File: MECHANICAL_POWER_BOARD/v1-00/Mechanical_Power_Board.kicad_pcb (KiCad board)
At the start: 2 copper layers, 180.4 x 44.5 mm, 46 parts, among them K1 COLONETTE, K10 CONN_3, K11 CONN_3, K12 CONN_3, K13 CONN_3, K14 CONN_3, K15 CONN_3, K16 CONN_3, K17 CONN_3, K18 CONN_3, K19 CONN_3, K2 COLONETTE, K20 CONN_3, K3 COLONETTE, K4 COLONETTE, K5 COLONETTE, K6 COLONETTE, K7 COLONETTE, K8 COLONETTE, K9 CONN_3, P1 CONN_12, P10 CONN_4, P11 CONN_4, P12 CONN_6, P13 CONN_6, P14 CONN_8, P15 CONN_8X2, P16 CONN_6, P17 CONN_8X2, P18 CONN_5X2, P19 CONN_5X2, P2 HE10-40, P3 CONN_4, P4 CONN_4, P5 CONN_4, P6 CONN_4

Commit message: Mechanical Power Board V1-00 ready for production
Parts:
- removed P14: CONN_8, KK-8-H
- removed P16: CONN_6, WEIDMULLER6
- added D6: 3V6, Diodes_SMD:MELF_Handsoldering, B.Cu at (107.3, 43.9)
- added D7: 5V6, Diodes_SMD:MELF_Handsoldering, B.Cu at (103.8, 43.9)
- added D8: 5V6, Diodes_SMD:MELF_Handsoldering, B.Cu at (100.2, 43.9)
- added D9: 13V, Diodes_SMD:MELF_Handsoldering, B.Cu at (96.6, 43.9)
- added K21: CONN_2, CEN-PCB:KK-2, F.Cu at (134.0, 52.1)
- added K22: CONN_2, CEN-PCB:KK-2, F.Cu at (148.0, 52.1)
- added K23: CONN_3, CEN-PCB:KK-3, F.Cu at (155.6, 52.1)
- added K24: CONN_3, CEN-PCB:KK-3, F.Cu at (141.6, 52.1)
- R1: value 1K -> 4.7k
- R2: value 820 -> 4.7k
- R3: value 680 -> 1.5k
- R4: value 330 -> 1.5k
- R5: value 220 -> 680
- moved P12 18.7 mm to (110.7, 66.6), turned to 180 degrees
- moved P13 17.5 mm to (85.9, 66.5), turned to 180 degrees
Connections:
- D5 pad 1: +3.3V -> +3V3
- P1 pad 10: +5VD -> +5V
- P1 pad 11: +3.3V -> +12V
- P1 pad 12: GND -> +15V
- P1 pad 7: +15V -> GND
- P1 pad 8: +12V -> +3V3
- P1 pad 9: +5V -> +5VD
- P12 pad 2: +3.3V -> +3V3
- P13 pad 2: +3.3V -> +3V3
- P15 pad 3: +3.3V -> +3V3
- P15 pad 4: +3.3V -> +3V3
- P17 pad 3: +3.3V -> +3V3
- P17 pad 4: +3.3V -> +3V3
- P2 pad 18: /IRQ1 -> (no net)
- P2 pad 20: /IRQ2 -> (no net)
- P2 pad 32: N-0000050 -> /IRQ2
- P2 pad 7: N-0000048 -> (no net)
- P2 pad 8: N-0000049 -> (no net)
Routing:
- net +3.3V: track 223.5 -> 0.00 mm, vias 3 -> 0
- net +3V3: track 0.00 -> 196.4 mm, vias 0 -> 3
- net GND: track 497.7 -> 571.2 mm, vias 3 -> 2
- net +15V: track 233.9 -> 199.0 mm, vias 3 -> 4
- net /RST: track 174.4 -> 201.7 mm, vias 4 -> 3
- net +12V: track 347.0 -> 373.1 mm
- net /A1: track 67.4 -> 47.2 mm, vias 2 -> 1
- net /IRQ2: track 105.8 -> 92.0 mm
- net /B2: track 46.3 -> 59.1 mm, vias 0 -> 2
- net /B1: track 54.6 -> 42.1 mm, vias 2 -> 1
- net +5VD: track 231.3 -> 220.8 mm, vias 6 -> 5
- net /Z1: track 46.4 -> 37.0 mm, vias 0 -> 1
- net /Z2: track 59.9 -> 53.4 mm
- net /A2: track 54.4 -> 59.2 mm, vias 2 -> 0
- net +5V: track 271.7 -> 275.0 mm, vias 7 -> 8
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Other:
- board text added: "MECHANICAL POWER BRD V1-00 OCT 15 F4DEB"
- board text removed: "+12"
- board text removed: "F4DEB"
- board text removed: "GND"
- board text removed: "MECHANICAL POWER BOARD V1-00"

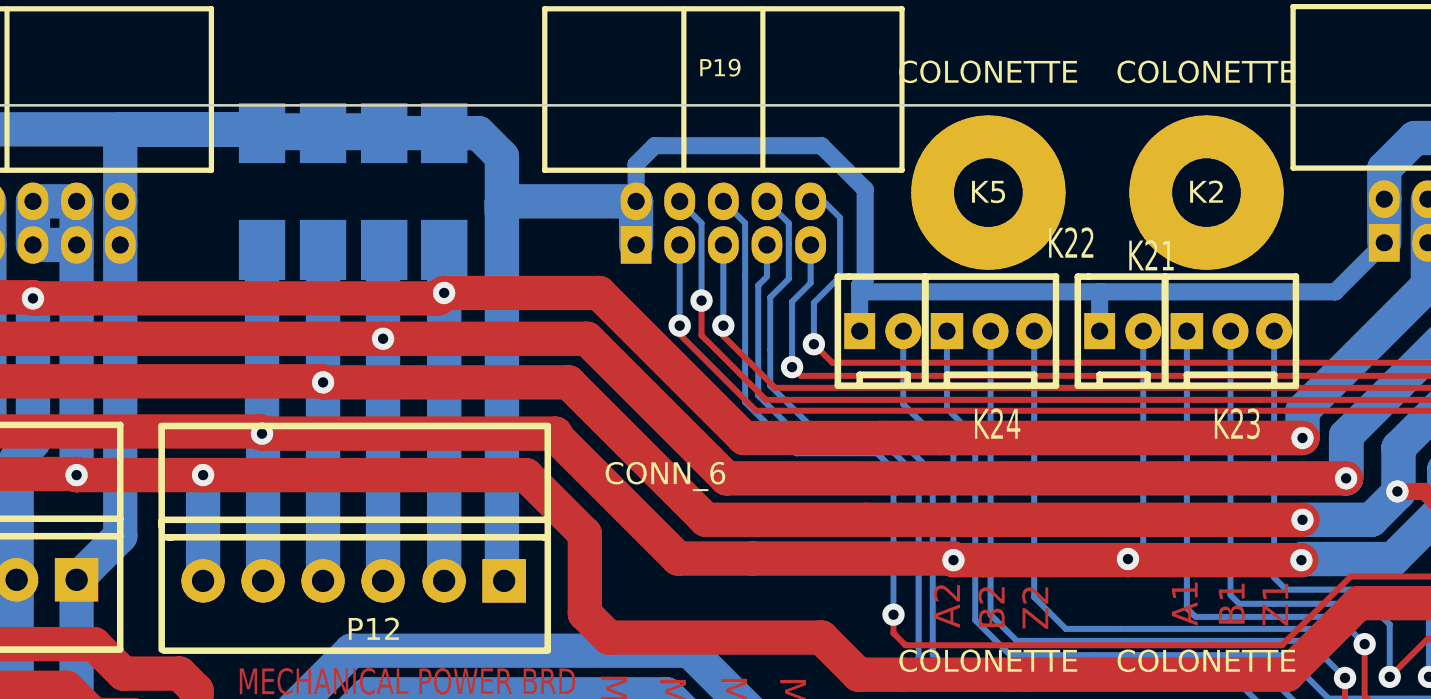
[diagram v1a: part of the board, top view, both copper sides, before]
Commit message: test mechanicalmotorboard PCB NOK
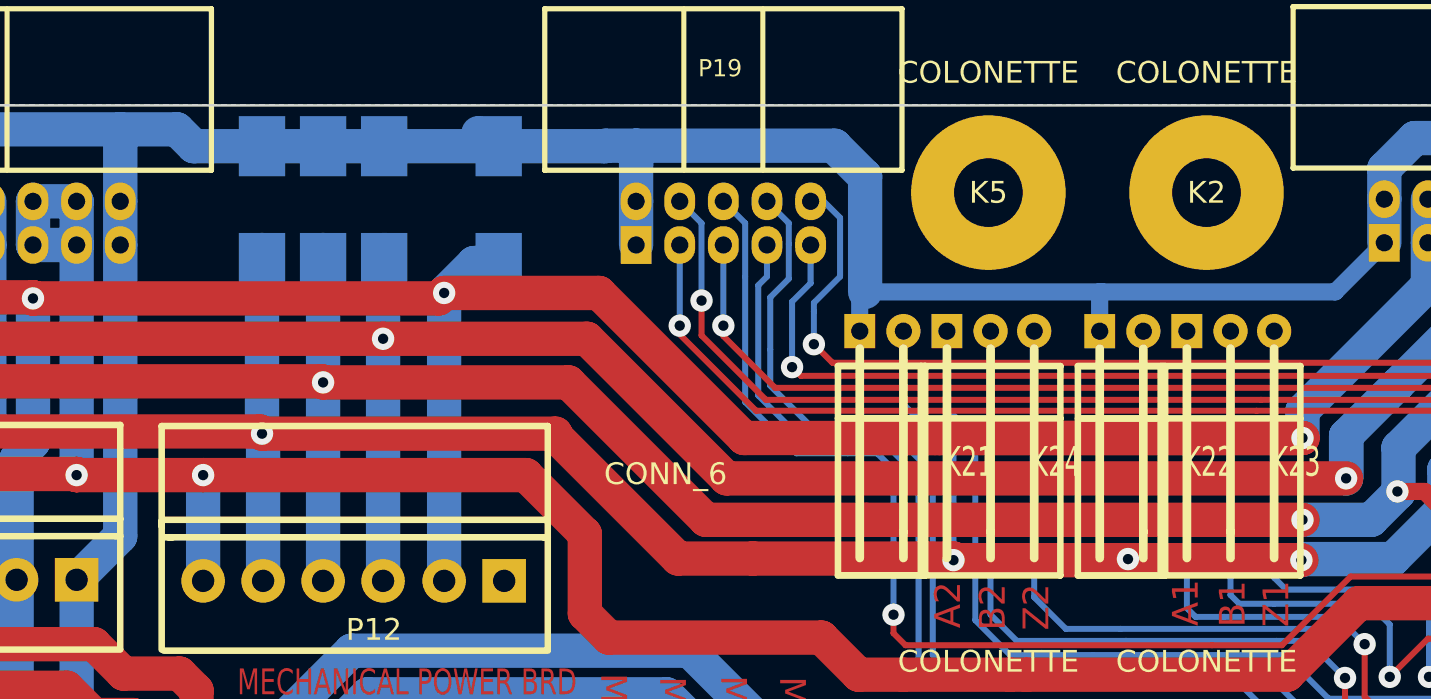
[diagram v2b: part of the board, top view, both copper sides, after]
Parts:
- K21, K22: footprint CEN-PCB:KK-2 -> f4deb-mod-library:KK-2-H
- K23, K24: footprint CEN-PCB:KK-3 -> CEN-PCB:SIL-3%221%2f2-3-HOR
- moved D6 3.27 mm to (110.4, 44.7)
- moved D7 0.76 mm to (103.8, 44.7)
- moved D8 0.76 mm to (100.2, 44.7)
- moved D9 0.76 mm to (96.6, 44.7)
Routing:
- net GND: track 571.2 -> 554.9 mm
- net +3V3: track 196.4 -> 197.8 mm
